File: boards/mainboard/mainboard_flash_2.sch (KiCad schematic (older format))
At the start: 2 parts, among them U1001 SST26VF064B

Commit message: [mainboard] update connectors, select most footprints; docs: update SVGs
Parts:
- C1001: footprint (none) -> Capacitors_SMD:C_0603
- U1001: footprint (none) -> Housings_SOIC:SOIC-8_3.9x4.9mm_Pitch1.27mm
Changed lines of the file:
@@
 F 0 "U1001" H 5750 3850 60  0000 C CNN
 F 1 "SST26VF064B" H 5750 4450 60  0000 C CNN
-F 2 "" H 5750 4150 60  0001 C CNN
+F 2 "Housings_SOIC:SOIC-8_3.9x4.9mm_Pitch1.27mm" H 5750 4150 60  0001 C CNN
 F 3 "" H 5750 4150 60  0001 C CNN
 	1    5750 4150
@@
 F 0 "C1001" H 4675 4300 50  0000 L CNN
 F 1 "100n" H 4675 4100 50  0000 L CNN
-F 2 "" H 4688 4050 50  0000 C CNN
+F 2 "Capacitors_SMD:C_0603" H 4688 4050 50  0001 C CNN
 F 3 "" H 4650 4200 50  0000 C CNN
 	1    4650 4200
@@
 $EndComp
 $Comp
-L +3V3 #PWR1005
+L +3V3 #PWR0109
 U 1 1 58FCEDE7
 P 6400 3900
-F 0 "#PWR1005" H 6400 3750 50  0001 C CNN
+F 0 "#PWR0109" H 6400 3750 50  0001 C CNN
 F 1 "+3V3" H 6400 4040 50  0000 C CNN
 F 2 "" H 6400 3900 50  0000 C CNN
@@
 $EndComp
 $Comp
-L +3V3 #PWR1001
+L +3V3 #PWR0110
 U 1 1 58FFF5F3
 P 4650 3950
-F 0 "#PWR1001" H 4650 3800 50  0001 C CNN
+F 0 "#PWR0110" H 4650 3800 50  0001 C CNN
 F 1 "+3V3" H 4650 4090 50  0000 C CNN
 F 2 "" H 4650 3950 50  0000 C CNN
@@
 $EndComp
 $Comp
-L GND #PWR1004
+L GND #PWR0111
 U 1 1 58FFF5F4
 P 5100 4400
-F 0 "#PWR1004" H 5100 4150 50  0001 C CNN
+F 0 "#PWR0111" H 5100 4150 50  0001 C CNN
 F 1 "GND" H 5100 4250 50  0000 C CNN
 F 2 "" H 5100 4400 50  0000 C CNN
@@
 $EndComp
 $Comp
-L GND #PWR1002
+L GND #PWR0112
 U 1 1 58FFF5F5
 P 4650 4450
-F 0 "#PWR1002" H 4650 4200 50  0001 C CNN
+F 0 "#PWR0112" H 4650 4200 50  0001 C CNN
 F 1 "GND" H 4650 4300 50  0000 C CNN
 F 2 "" H 4650 4450 50  0000 C CNN
@@
 $EndComp
 $Comp
-L +3V3 #PWR1003
+L +3V3 #PWR0113
 U 1 1 58FFF5F6
 P 5100 4200
-F 0 "#PWR1003" H 5100 4050 50  0001 C CNN
+F 0 "#PWR0113" H 5100 4050 50  0001 C CNN
 F 1 "+3V3" H 5100 4340 50  0000 C CNN
 F 2 "" H 5100 4200 50  0000 C CNN

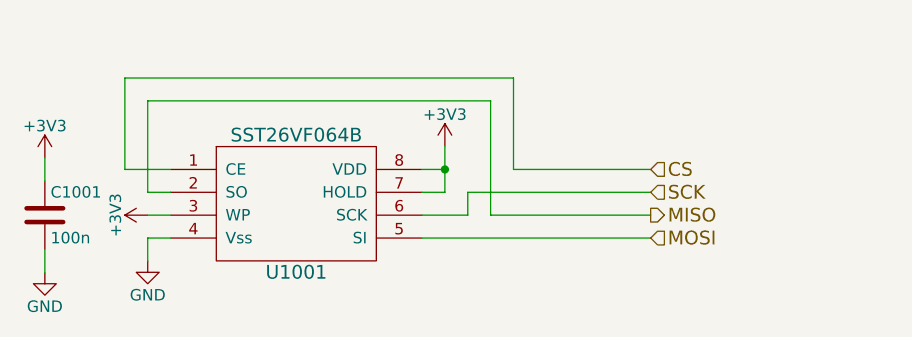
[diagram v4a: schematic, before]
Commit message: [mainboard] add test points
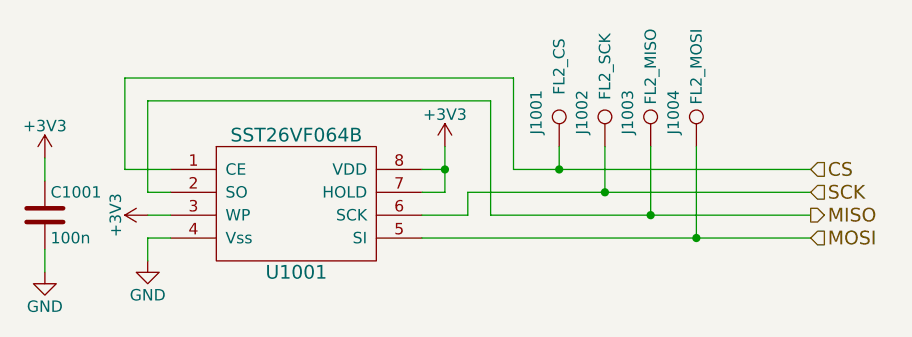
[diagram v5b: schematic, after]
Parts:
- added J1001: FL2_CS, Measurement_Points:Measurement_Point_Round-SMD-Pad_Small, symbol TEST_1P
- added J1002: FL2_SCK, Measurement_Points:Measurement_Point_Round-SMD-Pad_Small, symbol TEST_1P
- added J1003: FL2_MISO, Measurement_Points:Measurement_Point_Round-SMD-Pad_Small, symbol TEST_1P
- added J1004: FL2_MOSI, Measurement_Points:Measurement_Point_Round-SMD-Pad_Small, symbol TEST_1P
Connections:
- net CS: now also J1001.1
- net MISO: now also J1003.1
- net MOSI: now also J1004.1
- net SCK: now also J1002.1
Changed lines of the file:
@@
 	5100 4300 5200 4300
-Wire Wire Line
-	7300 4200 6600 4200
 Wire Wire Line
 	6600 3700 5100 3700
@@
 	6600 4200 6600 3700
 Wire Wire Line
-	6500 4100 7300 4100
-Wire Wire Line
 	6400 4100 6300 4100
 Connection ~ 6400 4000
@@
 	6700 3600 6700 4000
 Wire Wire Line
-	6700 4000 7300 4000
-Wire Wire Line
 	5000 3600 5000 4000
 Wire Wire Line
@@
 	5100 4200 5200 4200
 Wire Wire Line
-	6300 4300 7300 4300
-Wire Wire Line
 	6400 3900 6400 4100
 Wire Wire Line
@@
 Wire Wire Line
 	5100 4100 5200 4100
-Text HLabel 7300 4000 2    60   Input ~ 0
+Wire Wire Line
+	6600 4200 8000 4200
+Wire Wire Line
+	6500 4100 8000 4100
+Wire Wire Line
+	6700 4000 8000 4000
+Wire Wire Line
+	6300 4300 8000 4300
+Text HLabel 8000 4000 2    60   Input ~ 0
 CS
-Text HLabel 7300 4100 2    60   Input ~ 0
+Text HLabel 8000 4100 2    60   Input ~ 0
 SCK
-Text HLabel 7300 4300 2    60   Input ~ 0
+Text HLabel 8000 4300 2    60   Input ~ 0
 MOSI
-Text HLabel 7300 4200 2    60   Output ~ 0
+Text HLabel 8000 4200 2    60   Output ~ 0
 MISO
+$Comp
+L TEST_1P J1001
+U 1 1 5917578E
+P 6900 3900
+F 0 "J1001" V 6800 4050 50  0000 C CNN
+F 1 "FL2_CS" V 6900 4250 50  0000 C CNN
+F 2 "Measurement_Points:Measurement_Point_Round-SMD-Pad_Small" H 7100 3900 50  0001 C CNN
+F 3 "" H 7100 3900 50  0001 C CNN
+	1    6900 3900
+	1    0    0    -1
+$EndComp
+$Comp
+L TEST_1P J1002
+U 1 1 59175795
+P 7100 3900
+F 0 "J1002" V 7000 4050 50  0000 C CNN
+F 1 "FL2_SCK" V 7100 4250 50  0000 C CNN
+F 2 "Measurement_Points:Measurement_Point_Round-SMD-Pad_Small" H 7300 3900 50  0001 C CNN
+F 3 "" H 7300 3900 50  0001 C CNN
+	1    7100 3900
+	1    0    0    -1
+$EndComp
+$Comp
+L TEST_1P J1003
+U 1 1 5917579C
+P 7300 3900
+F 0 "J1003" V 7200 4050 50  0000 C CNN
+F 1 "FL2_MISO" V 7300 4250 50  0000 C CNN
+F 2 "Measurement_Points:Measurement_Point_Round-SMD-Pad_Small" H 7500 3900 50  0001 C CNN
+F 3 "" H 7500 3900 50  0001 C CNN
+	1    7300 3900
+	1    0    0    -1
+$EndComp
+$Comp
+L TEST_1P J1004
+U 1 1 591757A3
+P 7500 3900
+F 0 "J1004" V 7400 4050 50  0000 C CNN
+F 1 "FL2_MOSI" V 7500 4250 50  0000 C CNN
+F 2 "Measurement_Points:Measurement_Point_Round-SMD-Pad_Small" H 7700 3900 50  0001 C CNN
+F 3 "" H 7700 3900 50  0001 C CNN
+	1    7500 3900
+	1    0    0    -1
+$EndComp
+Wire Wire Line
+	6900 3900 6900 4000
+Connection ~ 6900 4000
+Wire Wire Line
+	7100 3900 7100 4100
+Connection ~ 7100 4100
+Wire Wire Line
+	7300 3900 7300 4200
+Connection ~ 7300 4200
+Wire Wire Line
+	7500 3900 7500 4300
+Connection ~ 7500 4300
 $EndSCHEMATC
